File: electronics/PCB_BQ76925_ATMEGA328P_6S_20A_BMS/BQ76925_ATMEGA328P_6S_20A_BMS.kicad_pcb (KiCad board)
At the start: 2 copper layers, 47 x 84 mm, 79 parts, among them J1 Conn_01x01, J2 Conn_01x01, J3 Conn_01x09, J4 Conn_01x02, J5 Conn_02x03, J6 Conn_01x04, Q1 BC817, Q2 IRFB4110, Q3 IRFB4110, Q4 IRFB4110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

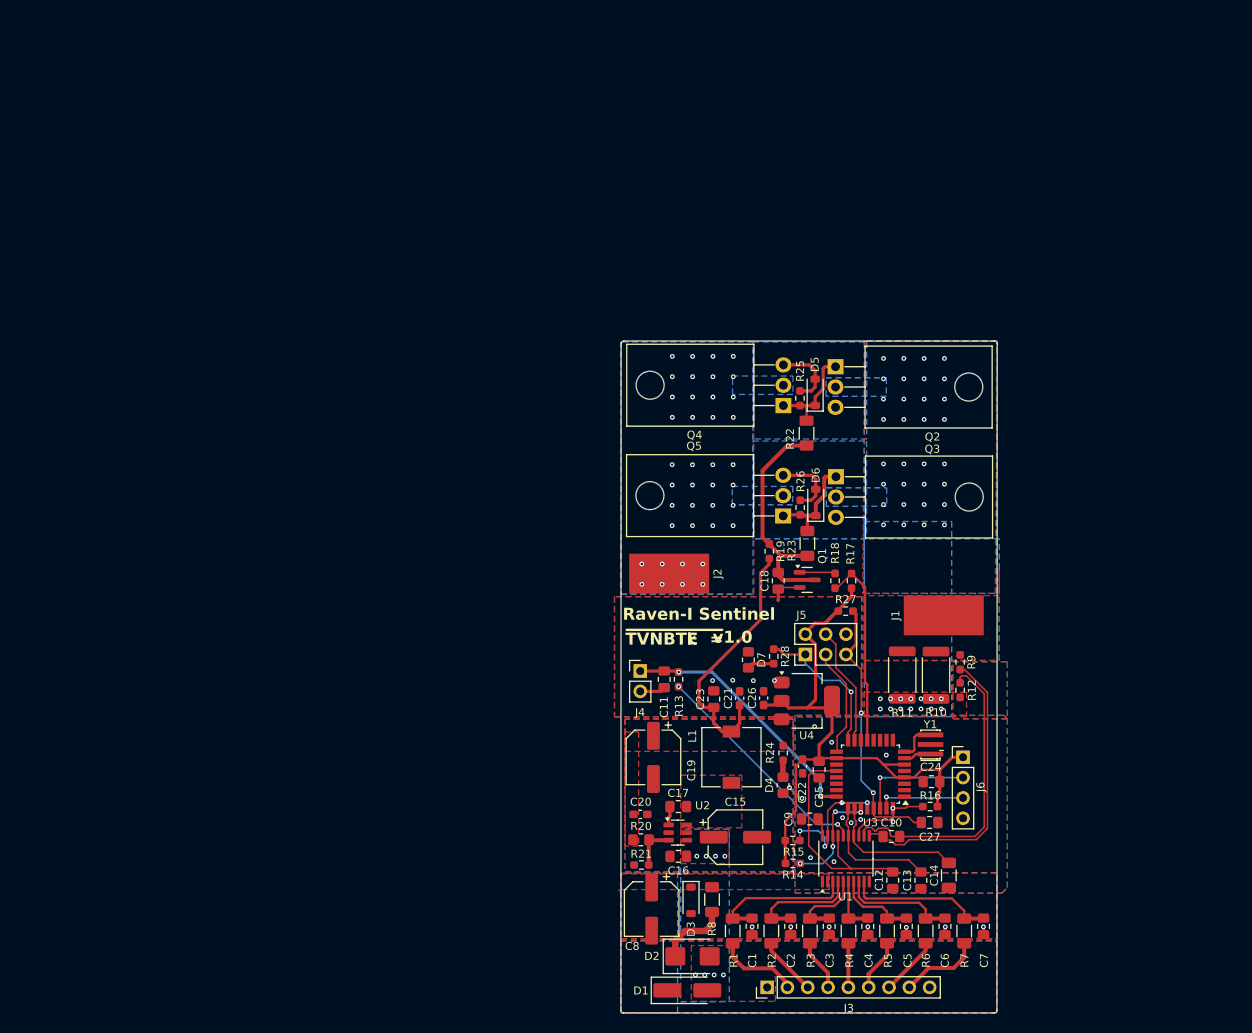
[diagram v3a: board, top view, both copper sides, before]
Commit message: completed pcb layout DRC completed. Final review and sleep with design pending
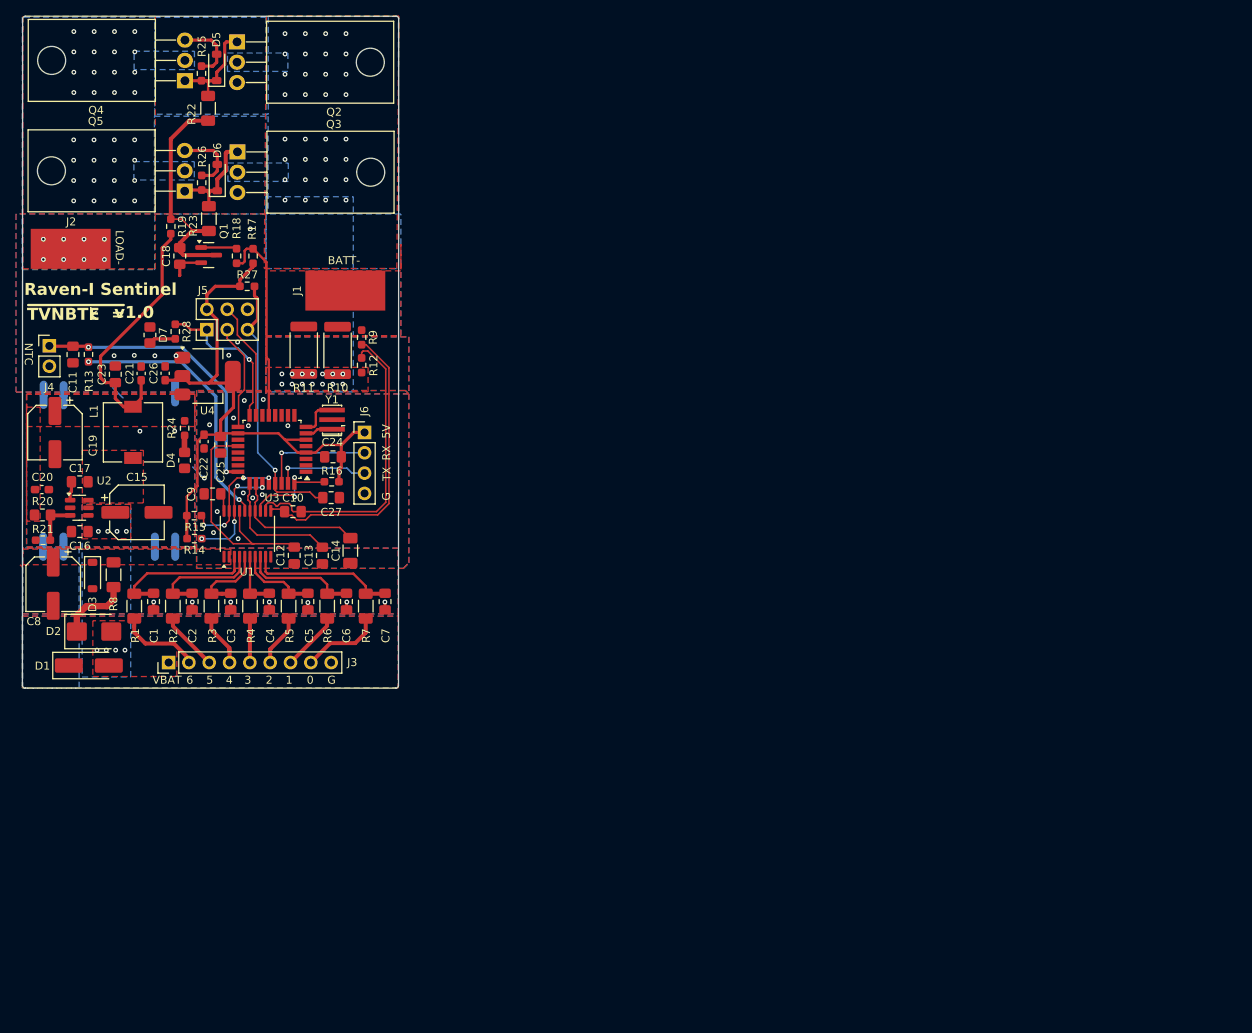
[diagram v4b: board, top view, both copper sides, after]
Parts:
- moved U4 85.2 mm to (63.9, 60.0)
- moved C10 85.1 mm to (74.5, 76.9)
- moved C25 85.1 mm to (65.5, 68.6)
- moved C27 85.1 mm to (79.3, 75.2)
- moved C12 85.1 mm to (74.7, 82.4)
- moved C13 85.1 mm to (78.2, 82.4)
- moved C16 85.1 mm to (47.9, 79.4)
- moved C17 85.1 mm to (47.9, 73.2)
- moved C18 85.1 mm to (60.4, 45.0)
- moved C19 85.1 mm to (44.8, 67.1)
- moved C20 85.1 mm to (43.2, 74.2)
- moved C21 85.1 mm to (55.6, 59.7)
- moved C23 85.1 mm to (52.3, 59.8)
- moved C26 85.1 mm to (58.6, 59.6)
- moved C3 85.1 mm to (66.7, 88.2)
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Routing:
- net GND: track 16.4 -> 32.8 mm, vias 21 -> 29
- net Net-(U1-VTB): track 28.7 -> 33.6 mm
- net /24V 6 Cell Monitoring/VTB: track 32.2 -> 36.0 mm
- net /24V 6 Cell Monitoring/SCL: track 15.8 -> 14.4 mm
- net +5V: track 82.6 -> 81.5 mm
- net /MCU/SW: track 24.5 -> 25.5 mm
- net +BATT: track 0.88 -> 0.00 mm
- net /MCU/TXD: track 11.0 -> 11.8 mm
- net /24V 6 Cell Monitoring/ALERT: track 11.2 -> 11.9 mm
- net /MCU/MISO: track 18.7 -> 19.4 mm
- net /24V 6 Cell Monitoring/SDA: track 13.2 -> 13.7 mm
- net /MCU/~{RESET}: track 33.9 -> 34.0 mm, vias 2 -> 1
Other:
- board text added: "0"
- board text added: "1"
- board text added: "2"
- board text added: "3"
- board text added: "4"
- board text added: "5"
- board text added: "5V"
- board text added: "6"
- board text added: "BATT-"
- board text added: "G"
- board text added: "LOAD-"
- board text added: "NTC"
- board text added: "RX"
- board text added: "TX"
- board text added: "VBAT"
- board text added: "~{TVNBTEk=}"
